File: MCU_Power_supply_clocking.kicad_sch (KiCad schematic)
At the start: 57 parts, among them J2 OSTTC020162, SW7 RESET, U10 TLV75529PDBV, U11 STM32H743ZIT6, U12 LD1117S33CTR, U13 LD1117S33CTR, U9 ST1L05APU33R, Y1 NX5032GA-8MHz, Y2 NX3215SA-32.768K-STD-MUA-14

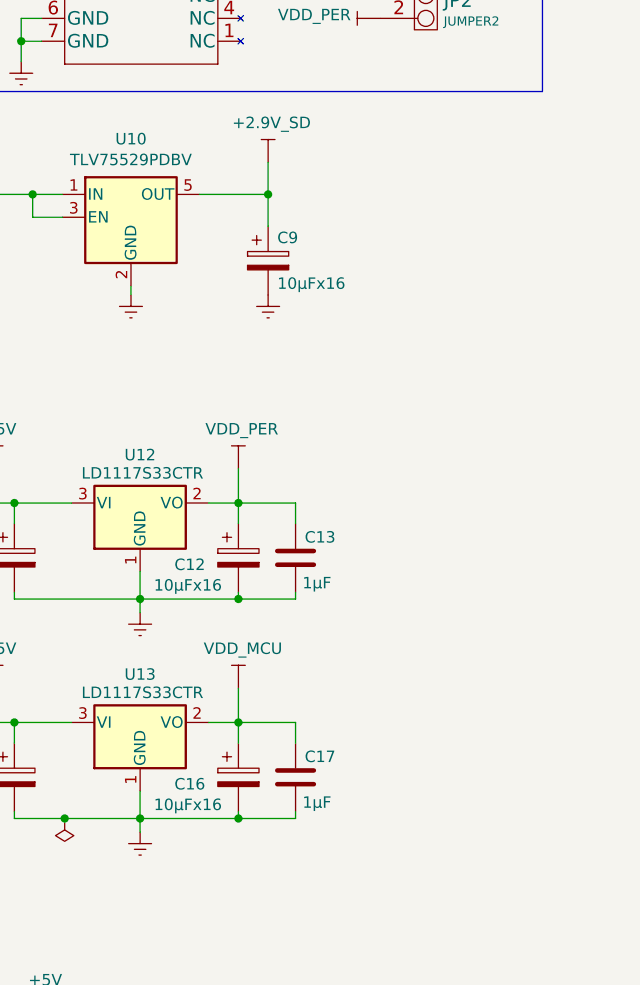
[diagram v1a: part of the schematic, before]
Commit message: Indication LEDs added
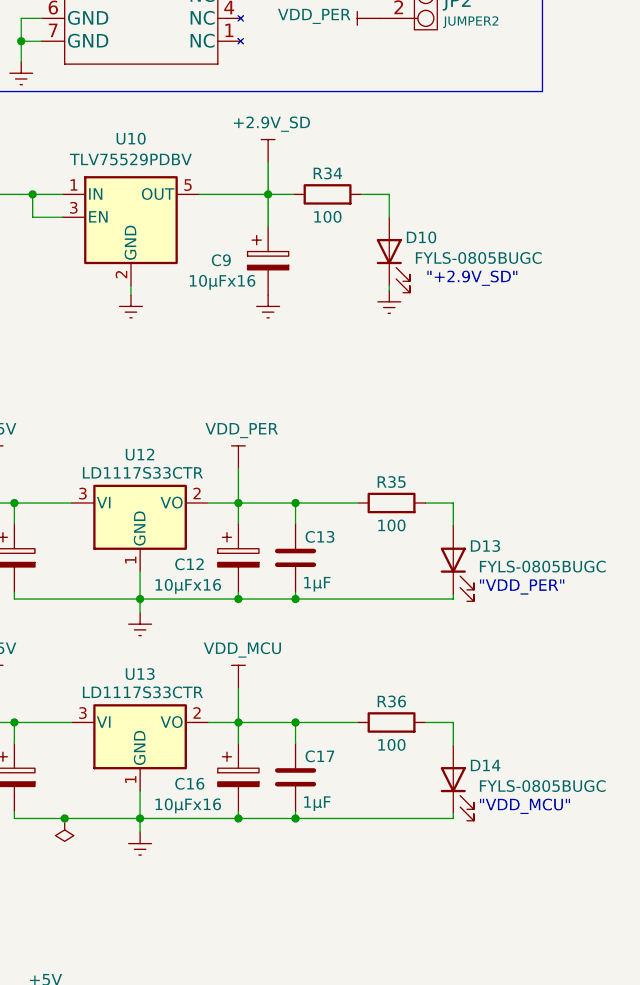
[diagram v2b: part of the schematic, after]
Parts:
- added D10, D13, D14: FYLS-0805BUGC, LED_SMD:LED_0805_2012Metric, symbol Device:LED
- added R34, R35, R36: 100, Resistor_SMD:R_0805_2012Metric, symbol Device:R
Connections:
- net +2,9V: now also R34.1
- net GNDREF: now also D10.1 (K), D13.1 (K), D14.1 (K)
- net VDD_MCU: now also R36.1
- net VDD_PER: now also R35.1
- new net: D13.2 (A), R35.2
- new net: D14.2 (A), R36.2
- new net: D10.2 (A), R34.2
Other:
- note added: ""+2.9V_SD""
- note added: ""VDD_MCU""
- note added: ""VDD_PER""
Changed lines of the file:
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@@
   (junction (at 201.93 59.944) (diameter 0) (color 0 0 0 0)
   )
+  (junction (at 237.998 104.902) (diameter 0) (color 0 0 0 0)
+  )
   (junction (at 18.034 49.53) (diameter 0) (color 0 0 0 0)
   )
@@
   (junction (at 71.882 44.45) (diameter 0) (color 0 0 0 0)
   )
+  (junction (at 237.998 129.286) (diameter 0) (color 0 0 0 0)
+  )
   (junction (at 82.042 154.94) (diameter 0) (color 0 0 0 0)
   )
@@
   (junction (at 60.706 154.94) (diameter 0) (color 0 0 0 0)
   )
+  (junction (at 237.998 118.618) (diameter 0) (color 0 0 0 0)
+  )
   (junction (at 18.034 67.31) (diameter 0) (color 0 0 0 0)
   )
+  (junction (at 237.998 94.234) (diameter 0) (color 0 0 0 0)
+  )
   (junction (at 67.818 141.732) (diameter 0) (color 0 0 0 0)
   )
@@
     (stroke (width 0) (type default) (color 0 0 0 0))
   )
+  (wire (pts (xy 252.476 94.234) (xy 255.524 94.234))
+    (stroke (width 0) (type default) (color 0 0 0 0))
+  )
   (wire (pts (xy 24.13 64.77) (xy 18.034 64.77))
     (stroke (width 0) (type default) (color 0 0 0 0))
@@
     (stroke (width 0) (type default) (color 0 0 0 0))
   )
+  (wire (pts (xy 248.412 70.612) (xy 248.412 70.104))
+    (stroke (width 0) (type default) (color 0 0 0 0))
+  )
   (wire (pts (xy 220.726 106.426) (xy 220.726 104.902))
     (stroke (width 0) (type default) (color 0 0 0 0))
@@
     (stroke (width 0) (type default) (color 0 0 0 0))
   )
+  (wire (pts (xy 237.998 129.286) (xy 255.524 129.286))
+    (stroke (width 0) (type default) (color 0 0 0 0))
+  )
   (wire (pts (xy 237.998 128.524) (xy 237.998 129.286))
     (stroke (width 0) (type default) (color 0 0 0 0))
@@
     (stroke (width 0) (type default) (color 0 0 0 0))
   )
+  (wire (pts (xy 245.364 59.944) (xy 248.412 59.944))
+    (stroke (width 0) (type default) (color 0 0 0 0))
+  )
   (wire (pts (xy 74.93 154.94) (xy 67.818 154.94))
     (stroke (width 0) (type default) (color 0 0 0 0))
@@
     (stroke (width 0) (type default) (color 0 0 0 0))
   )
+  (wire (pts (xy 252.476 118.618) (xy 255.524 118.618))
+    (stroke (width 0) (type default) (color 0 0 0 0))
+  )
   (wire (pts (xy 125.476 148.844) (xy 127.762 148.844))
     (stroke (width 0) (type default) (color 0 0 0 0))
   )
+  (wire (pts (xy 237.998 104.902) (xy 255.524 104.902))
+    (stroke (width 0) (type default) (color 0 0 0 0))
+  )
   (wire (pts (xy 33.02 112.776) (xy 33.02 115.316))
     (stroke (width 0) (type default) (color 0 0 0 0))
   )
+  (wire (pts (xy 255.524 96.774) (xy 255.524 94.234))
+    (stroke (width 0) (type default) (color 0 0 0 0))
+  )
   (wire (pts (xy 114.3 165.608) (xy 118.364 165.608))
     (stroke (width 0) (type default) (color 0 0 0 0))
@@
     (stroke (width 0) (type default) (color 0 0 0 0))
   )
+  (wire (pts (xy 255.524 129.286) (xy 255.524 128.778))
+    (stroke (width 0) (type default) (color 0 0 0 0))
+  )
   (wire (pts (xy 89.154 141.732) (xy 96.266 141.732))
     (stroke (width 0) (type default) (color 0 0 0 0))
   )
+  (wire (pts (xy 248.412 62.484) (xy 248.412 59.944))
+    (stroke (width 0) (type default) (color 0 0 0 0))
+  )
   (wire (pts (xy 53.34 185.42) (xy 53.34 182.626))
     (stroke (width 0) (type default) (color 0 0 0 0))
@@
     (stroke (width 0) (type default) (color 0 0 0 0))
   )
+  (wire (pts (xy 237.998 94.234) (xy 244.856 94.234))
+    (stroke (width 0) (type default) (color 0 0 0 0))
+  )
   (wire (pts (xy 122.682 185.674) (xy 122.682 178.308))
     (stroke (width 0) (type default) (color 0 0 0 0))
   )
+  (wire (pts (xy 234.95 59.944) (xy 237.744 59.944))
+    (stroke (width 0) (type default) (color 0 0 0 0))
+  )
   (wire (pts (xy 18.034 82.55) (xy 24.13 82.55))
     (stroke (width 0) (type default) (color 0 0 0 0))
@@
     (stroke (width 0) (type default) (color 0 0 0 0))
   )
+  (wire (pts (xy 255.524 104.902) (xy 255.524 104.394))
+    (stroke (width 0) (type default) (color 0 0 0 0))
+  )
   (wire (pts (xy 131.572 165.608) (xy 135.636 165.608))
     (stroke (width 0) (type default) (color 0 0 0 0))
@@
     (stroke (width 0) (type default) (color 0 0 0 0))
   )
+  (wire (pts (xy 237.998 118.618) (xy 244.856 118.618))
+    (stroke (width 0) (type default) (color 0 0 0 0))
+  )
   (wire (pts (xy 85.852 34.29) (xy 73.914 34.29))
     (stroke (width 0) (type default) (color 0 0 0 0))
@@
   )
   (wire (pts (xy 67.564 172.212) (xy 74.676 172.212))
+    (stroke (width 0) (type default) (color 0 0 0 0))
+  )
+  (wire (pts (xy 255.524 121.158) (xy 255.524 118.618))
     (stroke (width 0) (type default) (color 0 0 0 0))
   )
@@
   )
   (text "Backup LDO" (at 214.63 20.32 0)
+    (effects (font (size 1.27 1.27)) (justify left bottom))
+  )
+  (text "\"VDD_PER\"" (at 258.318 104.394 0)
+    (effects (font (size 1.27 1.27)) (justify left bottom))
+  )
+  (text "\"+2.9V_SD\"" (at 252.476 70.104 0)
+    (effects (font (size 1.27 1.27)) (justify left bottom))
+  )
+  (text "\"VDD_MCU\"" (at 258.318 128.778 0)
     (effects (font (size 1.27 1.27)) (justify left bottom))
   )
@@
   (symbol (lib_id "Device:CP") (at 234.95 67.31 0) (unit 1)
     (in_bom yes) (on_board yes)
-    (property "Reference" "C9" (id 0) (at 235.966 64.77 0)
-      (effects (font (size 1.27 1.27)) (justify left))
-    )
-    (property "Value" "10µFx16" (id 1) (at 235.966 69.85 0)
+    (property "Reference" "C9" (id 0) (at 228.6 67.31 0)
+      (effects (font (size 1.27 1.27)) (justify left))
+    )
+    (property "Value" "10µFx16" (id 1) (at 226.06 69.596 0)
       (effects (font (size 1.27 1.27)) (justify left))
     )
@@
     (pin "1")
   )
+  (symbol (lib_id "Device:LED") (at 255.524 100.584 90) (unit 1)
+    (in_bom yes) (on_board yes)
+    (property "Reference" "D13" (id 0) (at 259.08 99.06 90))
+    (property "Value" "FYLS-0805BUGC" (id 1) (at 265.43 101.346 90))
+    (property "Footprint" "LED_SMD:LED_0805_2012Metric" (id 2) (at 255.524 100.584 0)
+      (effects (font (size 1.27 1.27)) hide)
+    )
+    (property "Datasheet" "" (id 3) (at 255.524 100.584 0)
+      (effects (font (size 1.27 1.27)) hide)
+    )
+    (pin "1")
+    (pin "2")
+  )
+  (symbol (lib_id "Device:R") (at 248.666 118.618 90) (unit 1)
+    (in_bom yes) (on_board yes)
+    (property "Reference" "R36" (id 0) (at 248.666 116.332 90))
+    (property "Value" "100" (id 1) (at 248.666 121.158 90))
+    (property "Footprint" "Resistor_SMD:R_0805_2012Metric" (id 2) (at 248.666 120.396 90)
+      (effects (font (size 1.27 1.27)) hide)
+    )
+    (property "Datasheet" "~" (id 3) (at 248.666 118.618 0)
+      (effects (font (size 1.27 1.27)) hide)
+    )
+    (property "Type" "RC0805FR-07100RL" (id 4) (at 248.666 118.618 0)
+      (effects (font (size 1.27 1.27)) hide)
+    )
+    (pin "1")
+    (pin "2")
+  )
+  (symbol (lib_id "Device:LED") (at 255.524 124.968 90) (unit 1)
+    (in_bom yes) (on_board yes)
+    (property "Reference" "D14" (id 0) (at 259.08 123.444 90))
+    (property "Value" "FYLS-0805BUGC" (id 1) (at 265.43 125.73 90))
+    (property "Footprint" "LED_SMD:LED_0805_2012Metric" (id 2) (at 255.524 124.968 0)
+      (effects (font (size 1.27 1.27)) hide)
+    )
+    (property "Datasheet" "" (id 3) (at 255.524 124.968 0)
+      (effects (font (size 1.27 1.27)) hide)
+    )
+    (pin "1")
+    (pin "2")
+  )
+  (symbol (lib_id "power:GNDREF") (at 248.412 70.612 0) (unit 1)
+    (in_bom yes) (on_board yes)
+    (property "Reference" "#PWR074" (id 0) (at 248.412 76.962 0)
+      (effects (font (size 1.27 1.27)) hide)
+    )
+    (property "Value" "GNDREF" (id 1) (at 248.539 73.8632 90)
+      (effects (font (size 1.27 1.27)) (justify right) hide)
+    )
+    (property "Footprint" "" (id 2) (at 248.412 70.612 0)
+      (effects (font (size 1.27 1.27)) hide)
+    )
+    (property "Datasheet" "" (id 3) (at 248.412 70.612 0)
+      (effects (font (size 1.27 1.27)) hide)
+    )
+    (pin "1")
+  )
+  (symbol (lib_id "Device:R") (at 241.554 59.944 90) (unit 1)
+    (in_bom yes) (on_board yes)
+    (property "Reference" "R34" (id 0) (at 241.554 57.658 90))
+    (property "Value" "100" (id 1) (at 241.554 62.484 90))
+    (property "Footprint" "Resistor_SMD:R_0805_2012Metric" (id 2) (at 241.554 61.722 90)
+      (effects (font (size 1.27 1.27)) hide)
+    )
+    (property "Datasheet" "~" (id 3) (at 241.554 59.944 0)
+      (effects (font (size 1.27 1.27)) hide)
+    )
+    (property "Type" "RC0805FR-07100RL" (id 4) (at 241.554 59.944 0)
+      (effects (font (size 1.27 1.27)) hide)
+    )
+    (pin "1")
+    (pin "2")
+  )
+  (symbol (lib_id "Device:R") (at 248.666 94.234 90) (unit 1)
+    (in_bom yes) (on_board yes)
+    (property "Reference" "R35" (id 0) (at 248.666 91.948 90))
+    (property "Value" "100" (id 1) (at 248.666 96.774 90))
+    (property "Footprint" "Resistor_SMD:R_0805_2012Metric" (id 2) (at 248.666 96.012 90)
+      (effects (font (size 1.27 1.27)) hide)
+    )
+    (property "Datasheet" "~" (id 3) (at 248.666 94.234 0)
+      (effects (font (size 1.27 1.27)) hide)
+    )
+    (property "Type" "RC0805FR-07100RL" (id 4) (at 248.666 94.234 0)
+      (effects (font (size 1.27 1.27)) hide)
+    )
+    (pin "1")
+    (pin "2")
+  )
+  (symbol (lib_id "Device:LED") (at 248.412 66.294 90) (unit 1)
+    (in_bom yes) (on_board yes)
+    (property "Reference" "D10" (id 0) (at 251.968 64.77 90))
+    (property "Value" "FYLS-0805BUGC" (id 1) (at 258.318 67.056 90))
+    (property "Footprint" "LED_SMD:LED_0805_2012Metric" (id 2) (at 248.412 66.294 0)
+      (effects (font (size 1.27 1.27)) hide)
+    )
+    (property "Datasheet" "" (id 3) (at 248.412 66.294 0)
+      (effects (font (size 1.27 1.27)) hide)
+    )
+    (pin "1")
+    (pin "2")
+  )
 )

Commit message: All handsolder footprints removed
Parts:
- C10, C14, C18, C19, C20, C21, C22, C23, C24, C25, C26, C27, C29, C30, C31, C33, C35, C36, C37, C38, C39, C40, C41, C42, C5, C6, C7: footprint Capacitor_SMD:C_0603_1608Metric_Pad1.08x0.95mm_HandSolder -> Capacitor_SMD:C_0603_1608Metric
- L2: footprint Inductor_SMD:L_0805_2012Metric_Pad1.15x1.40mm_HandSolder -> Inductor_SMD:L_0805_2012Metric
- R16, R17, R18: footprint Resistor_SMD:R_0805_2012Metric_Pad1.20x1.40mm_HandSolder -> Resistor_SMD:R_0805_2012Metric
